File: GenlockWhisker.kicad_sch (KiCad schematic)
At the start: 28 parts, among them J1 HDBNC-J-P-XX-ST-EM1, Q1 MMBT3904, U1 LMH1980MM/NOPB

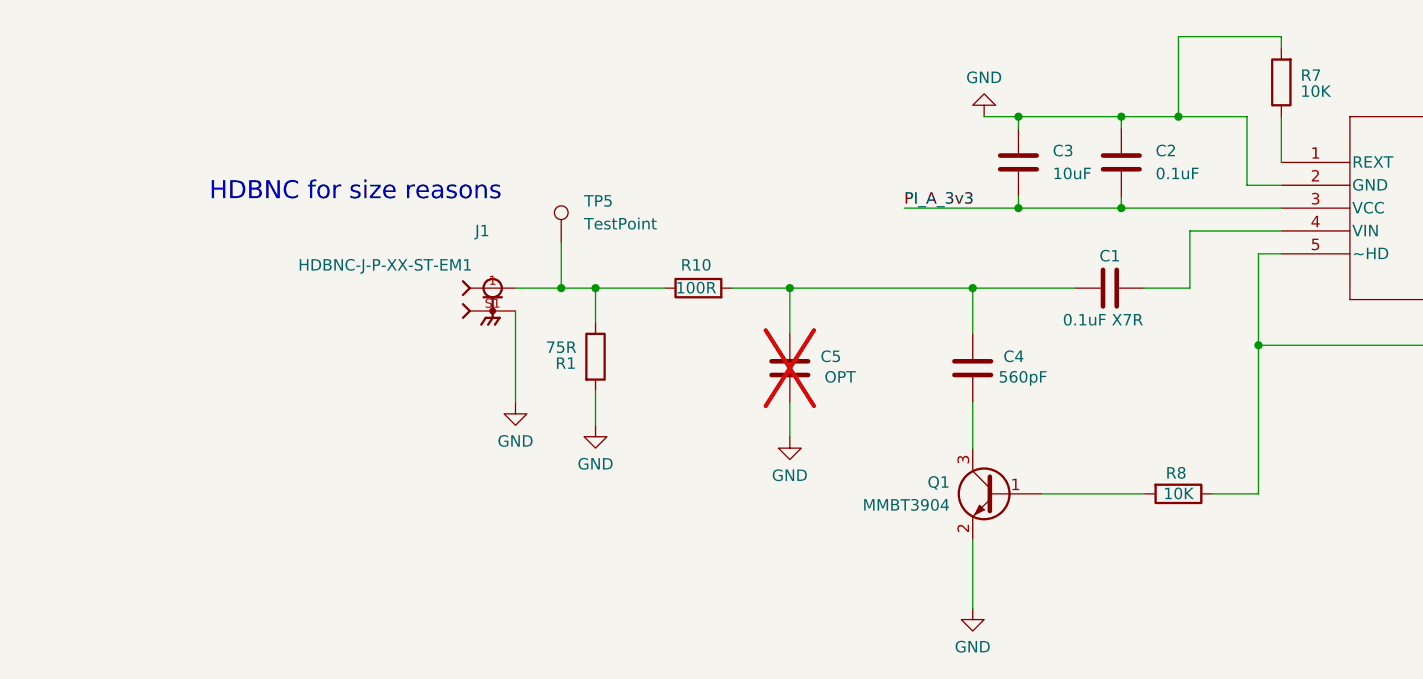
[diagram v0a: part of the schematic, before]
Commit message: New version with full size connector. major software improvements including high frequency logging and webserial UI
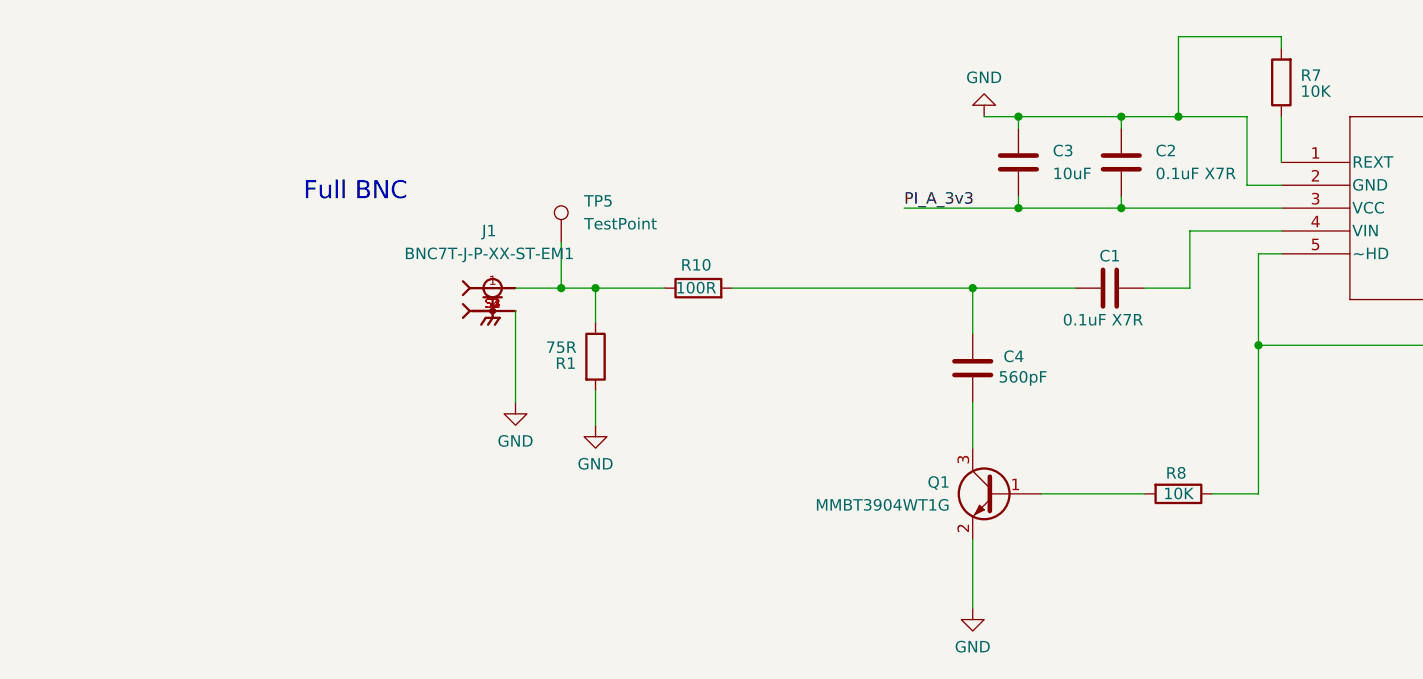
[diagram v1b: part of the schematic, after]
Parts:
- removed C5: OPT, Capacitor_SMD:C_0603_1608Metric, symbol Device:C
- removed J1: HDBNC-J-P-XX-ST-EM1, HDBNC-J-P-GN-ST-EM1:SAMTEC_HDBNC-J-P-XX-ST-EM1, symbol HDBNC-J-P-XX-ST-EM1:HDBNC-J-P-XX-ST-EM1
- added J1: BNC7T-J-P-XX-ST-EM1, BNC7T_J_P_GN_ST_EM1D-3:SAMTEC_BNC7T-J-P-XX-ST-EM1D, symbol BNC7T-J-P-XX-ST-EM1:BNC7T-J-P-XX-ST-EM1
- C1: Availability PROTOTYPE -> (none); LCSC (none) -> C14663
- C2: value 0.1uF -> 0.1uF X7R; Availability PROTOTYPE -> (none); LCSC (none) -> C14663
- C3: Availability PROTOTYPE -> (none); LCSC (none) -> C19702
- C4: Availability PROTOTYPE -> (none); LCSC (none) -> C1627
- H1, TP1, TP10, TP2, TP3, TP4, TP5, TP7, TP8, TP9, WIS3, WIS4: Availability (none) -> DNP; LCSC (none) -> DNP
- Q1: value MMBT3904 -> MMBT3904WT1G; LCSC (none) -> C58011
- R1: Availability PROTO-ONLY -> (none); LCSC (none) -> C4275
- R10, R4, R5, R6, R9: Availability PROTO-ONLY -> (none); LCSC (none) -> C22775
- R7, R8: Availability PROTO-ONLY -> (none); LCSC (none) -> C21190
- U1: LCSC (none) -> C189203
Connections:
- net GND: now also J1.S1, J1.S2, J1.S3, J1.S4
- net at R1.1, R10.1, TP5.1: now also J1.1
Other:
- note added: "Full BNC"
- note removed: "HDBNC for size reasons"
